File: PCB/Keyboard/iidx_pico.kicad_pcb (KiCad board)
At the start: 2 copper layers, 180 x 160 mm, 70 parts, among them J1 CONN_01x05, J2 CONN_01x05, SW1 SWITCH_SPST, SW10 SWITCH_SPST, SW11 SWITCH_SPST, SW12 Tact_4pin, SW13 Tact_4pin, SW2 SWITCH_SPST, SW3 SWITCH_SPST, SW4 SWITCH_SPST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

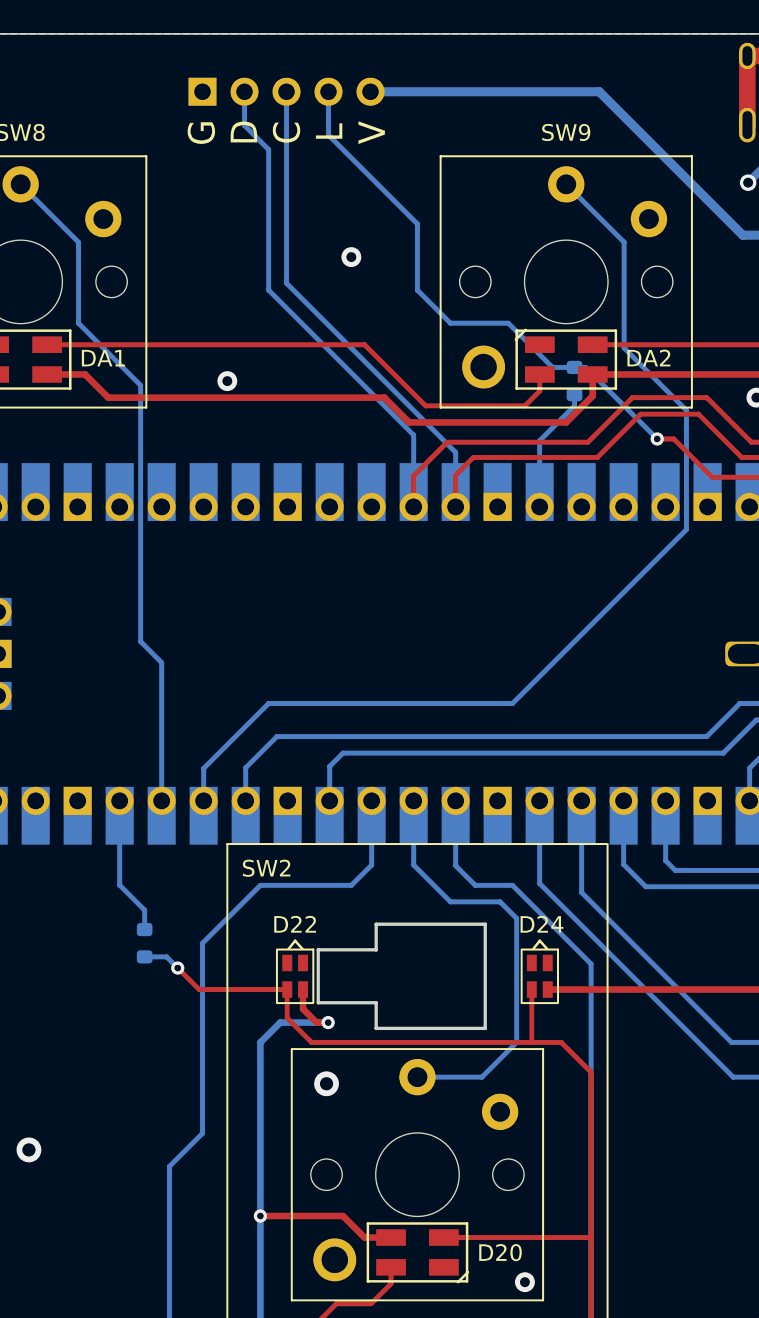
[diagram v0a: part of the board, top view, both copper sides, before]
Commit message: 3.3 to 5 level shifter added to PCB
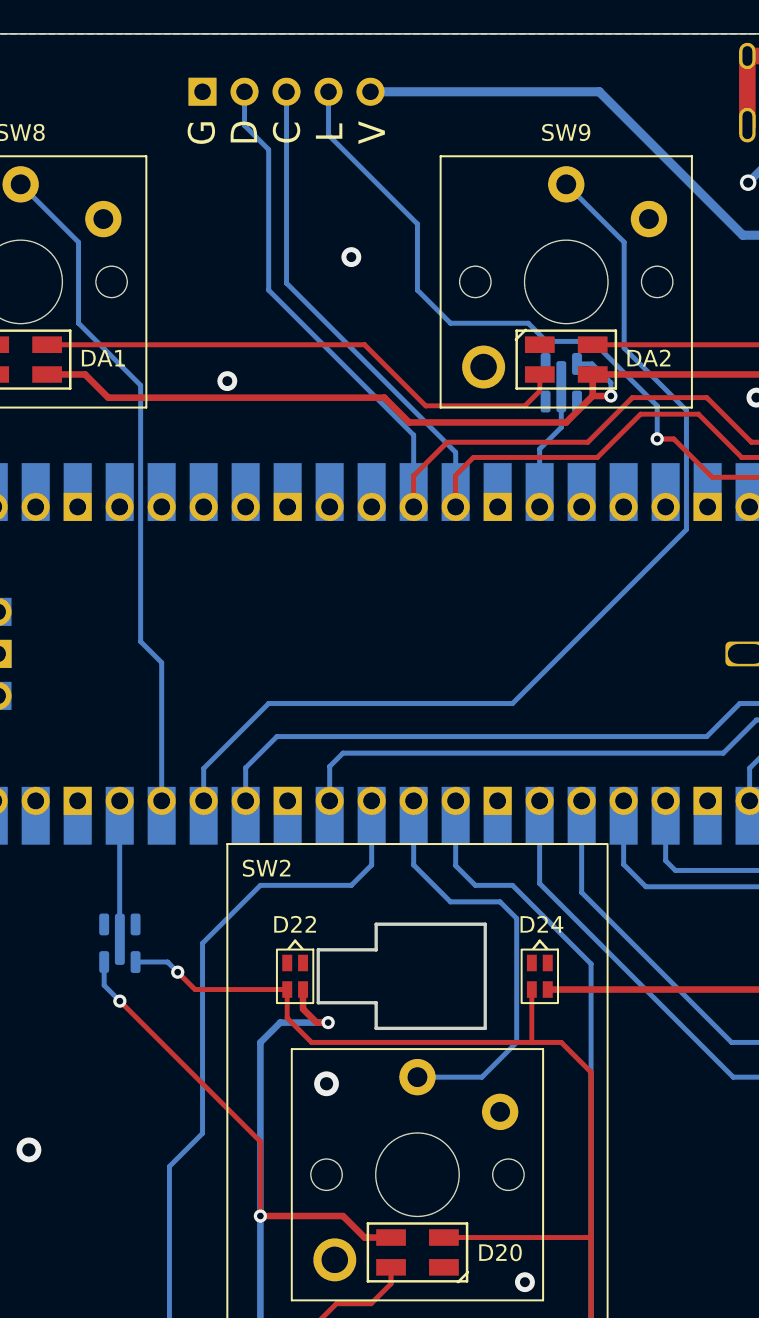
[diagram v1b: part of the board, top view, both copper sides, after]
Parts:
- removed R2, R3: 10, Resistor_SMD:R_0603_1608Metric
- added U2: SN74LV1T34DBV, iidx_pico:SOT-23-5_Jumper, B.Cu at (78.3, 74.4)
- added U3: SN74LV1T34DBV, iidx_pico:SOT-23-5_Jumper, B.Cu at (105.0, 40.5)
- R1: value 220 -> 10
- moved R1 109.3 mm to (183.8, 40.9), turned to -90 degrees
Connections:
- R1 pad 1: /LED2 -> Net-(DA4-PadO)
- R1 pad 2: Net-(R1-Pad2) -> /TT_LED
- U1 pad 17: Net-(R1-Pad2) -> Net-(U1-Pad17)
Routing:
- net +5V: track 1166.7 -> 1190.4 mm, vias 40 -> 42
- net Net-(R1-Pad2): track 8.41 -> 0.00 mm
- net Net-(U1-Pad17): track 0.00 -> 7.48 mm
- net /TT_LED: track 165.6 -> 168.1 mm
- net Net-(U1-Pad34): track 7.66 -> 6.92 mm

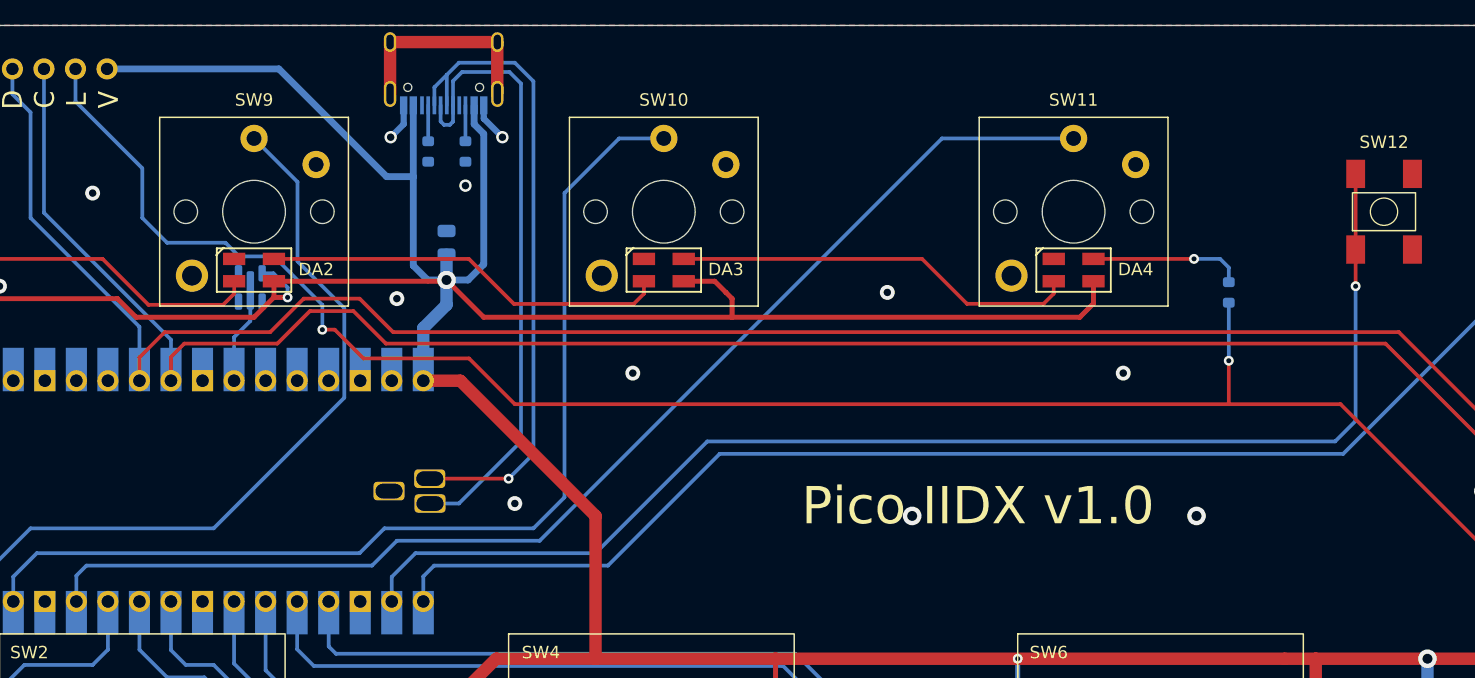
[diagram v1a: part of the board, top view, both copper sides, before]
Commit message: Adds 3.5mm 4P jack connection option
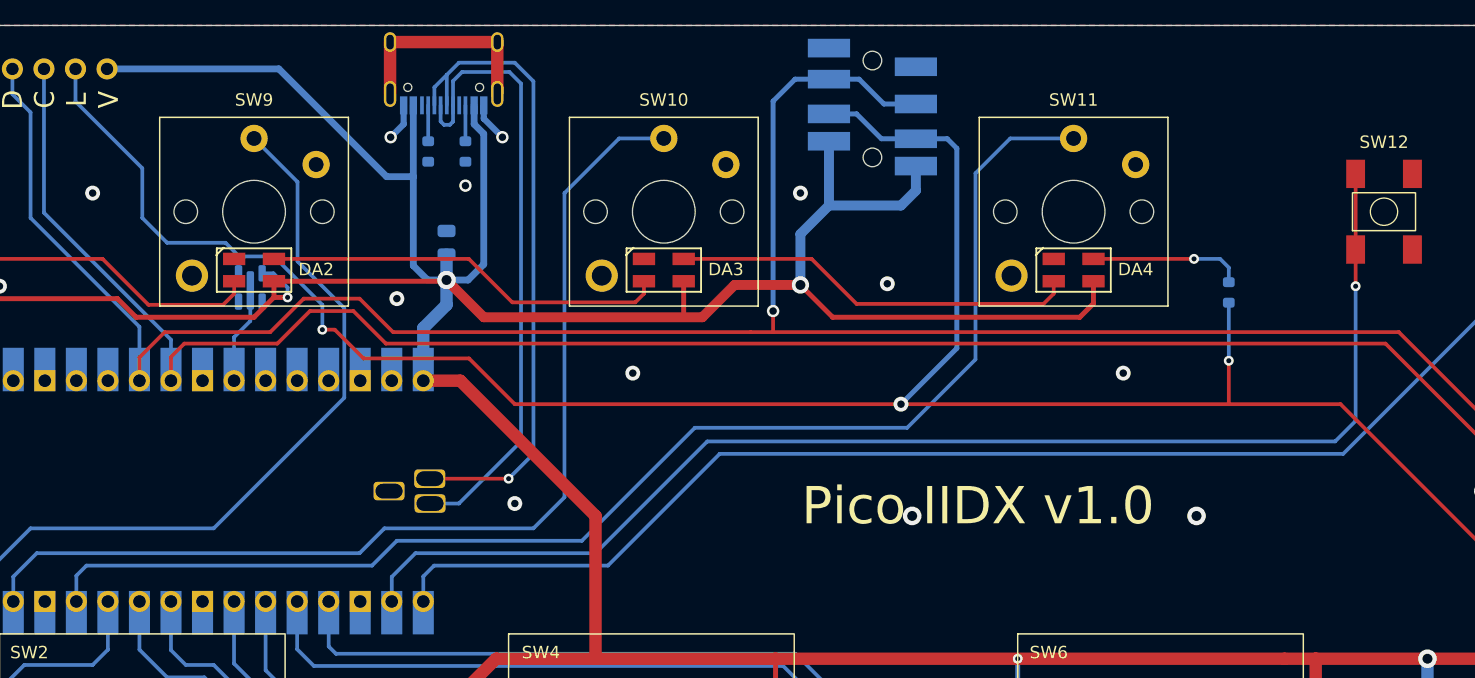
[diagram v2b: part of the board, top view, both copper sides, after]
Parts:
- added J3: PJ393-8P, iidx_pico:PJ393-8P, B.Cu at (155.1, 27.1)
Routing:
- net /TT_LED: track 168.1 -> 202.0 mm, vias 2 -> 3
- net /SDA: track 171.8 -> 203.5 mm, vias 0 -> 1
- net +5V: track 1190.4 -> 1211.5 mm, vias 42 -> 43
- net Net-(SW11-Pad1): track 97.0 -> 105.8 mm
- net GND: vias 46 -> 47

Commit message: PCB finetune a little bit
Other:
- board text added: "Pico IIDX v1.1"
- board text removed: "Pico IIDX v1.0"

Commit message: Add TVS diode and filter capacitor to PCB
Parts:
- added C6: 1uF, Capacitor_SMD:C_0805_2012Metric, B.Cu at (87.3, 38.9)
- added TV1: D_TVS, Diode_SMD:D_SOD-323_HandSoldering, B.Cu at (145.3, 49.9)
- added TV2: D_TVS, Diode_SMD:D_SOD-323_HandSoldering, B.Cu at (149.3, 49.9)
- added TV3: D_TVS, Diode_SMD:D_SOD-323_HandSoldering, B.Cu at (153.3, 49.9)
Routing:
- net /SDA: track 203.5 -> 212.1 mm
- net /TT_LED: track 202.0 -> 206.6 mm
- net /SCL: track 169.5 -> 173.1 mm, vias 0 -> 1
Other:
- board text added: "Pico IIDX v1.11"
- board text removed: "Pico IIDX v1.1"

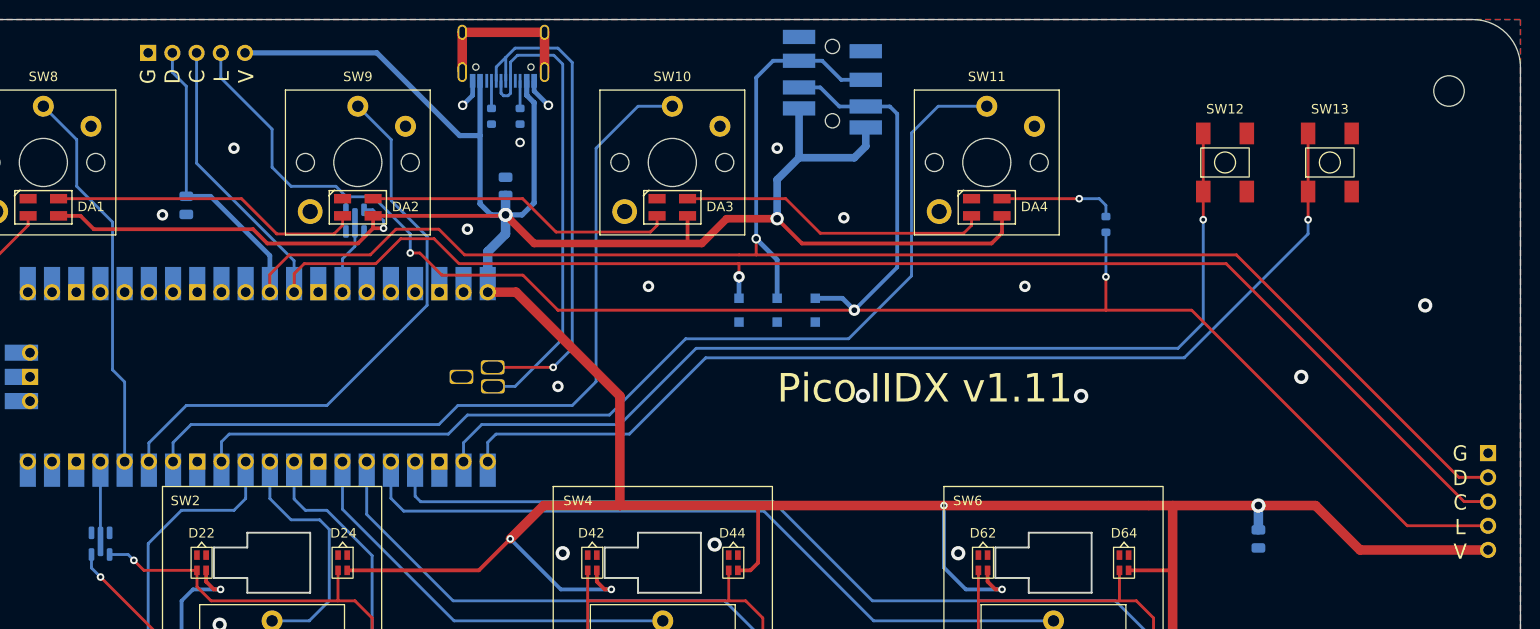
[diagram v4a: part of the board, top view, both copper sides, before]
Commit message: Resistors to bypass level shifter
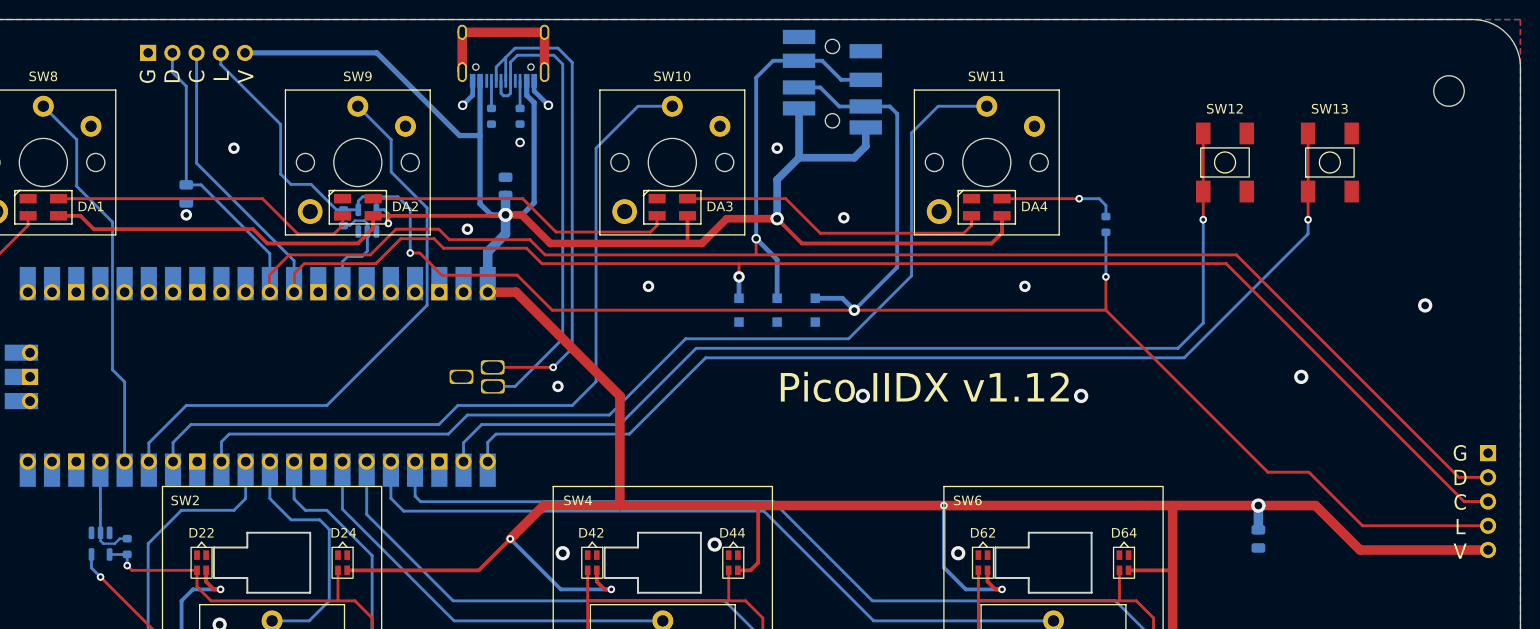
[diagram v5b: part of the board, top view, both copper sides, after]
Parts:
- added R2: 10, Resistor_SMD:R_0603_1608Metric, B.Cu at (81.1, 74.7)
- added R3: 10, Resistor_SMD:R_0603_1608Metric, B.Cu at (103.8, 40.2)
- C6: value 1uF -> 1nF
- moved U3 1.30 mm to (106.3, 40.5)
- moved C6 1.20 mm to (87.3, 37.7)
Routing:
- net Net-(U1-Pad34): track 6.92 -> 11.8 mm
- net Net-(U1-Pad17): track 7.48 -> 11.5 mm
- net /TT_LED: track 206.6 -> 208.4 mm
- net +5V: track 1211.5 -> 1210.3 mm
- net /LED2: track 88.6 -> 89.2 mm
- net /SDA: track 212.1 -> 211.5 mm
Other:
- board text added: "Pico IIDX v1.12"
- board text removed: "Pico IIDX v1.11"
